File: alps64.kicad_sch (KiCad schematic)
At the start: 27 parts, among them J2 USB_C_Receptacle, K18 keyboard_parts:KEYSW, K19 keyboard_parts:KEYSW, K28 keyboard_parts:KEYSW, K29 keyboard_parts:KEYSW, K8 keyboard_parts:KEYSW, K9 keyboard_parts:KEYSW, SW100 SW_PUSH, U1 32U2, X1 16MHz

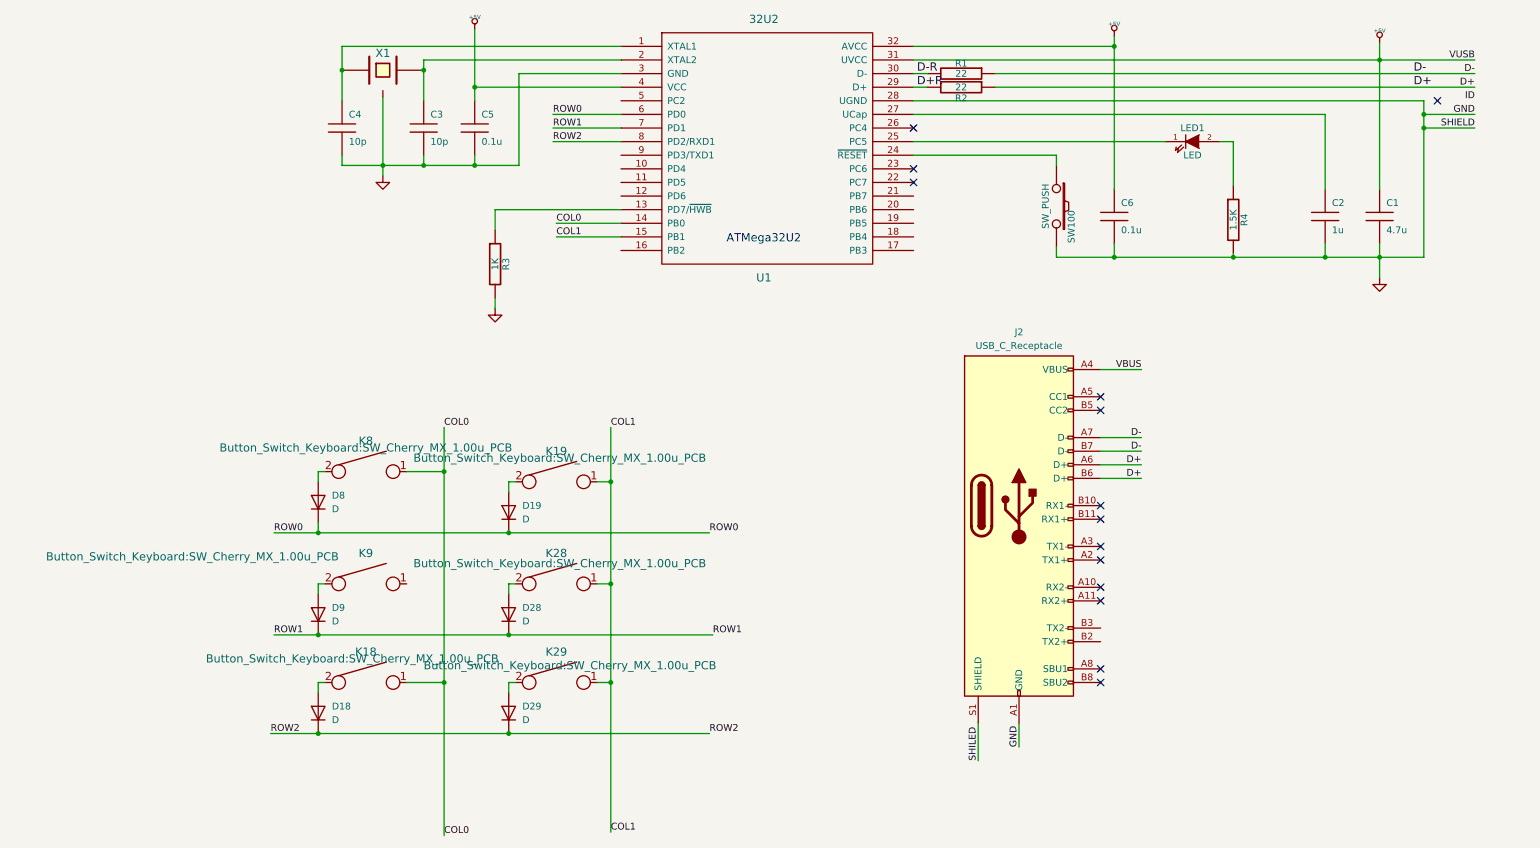
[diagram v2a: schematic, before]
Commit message: Update footprints
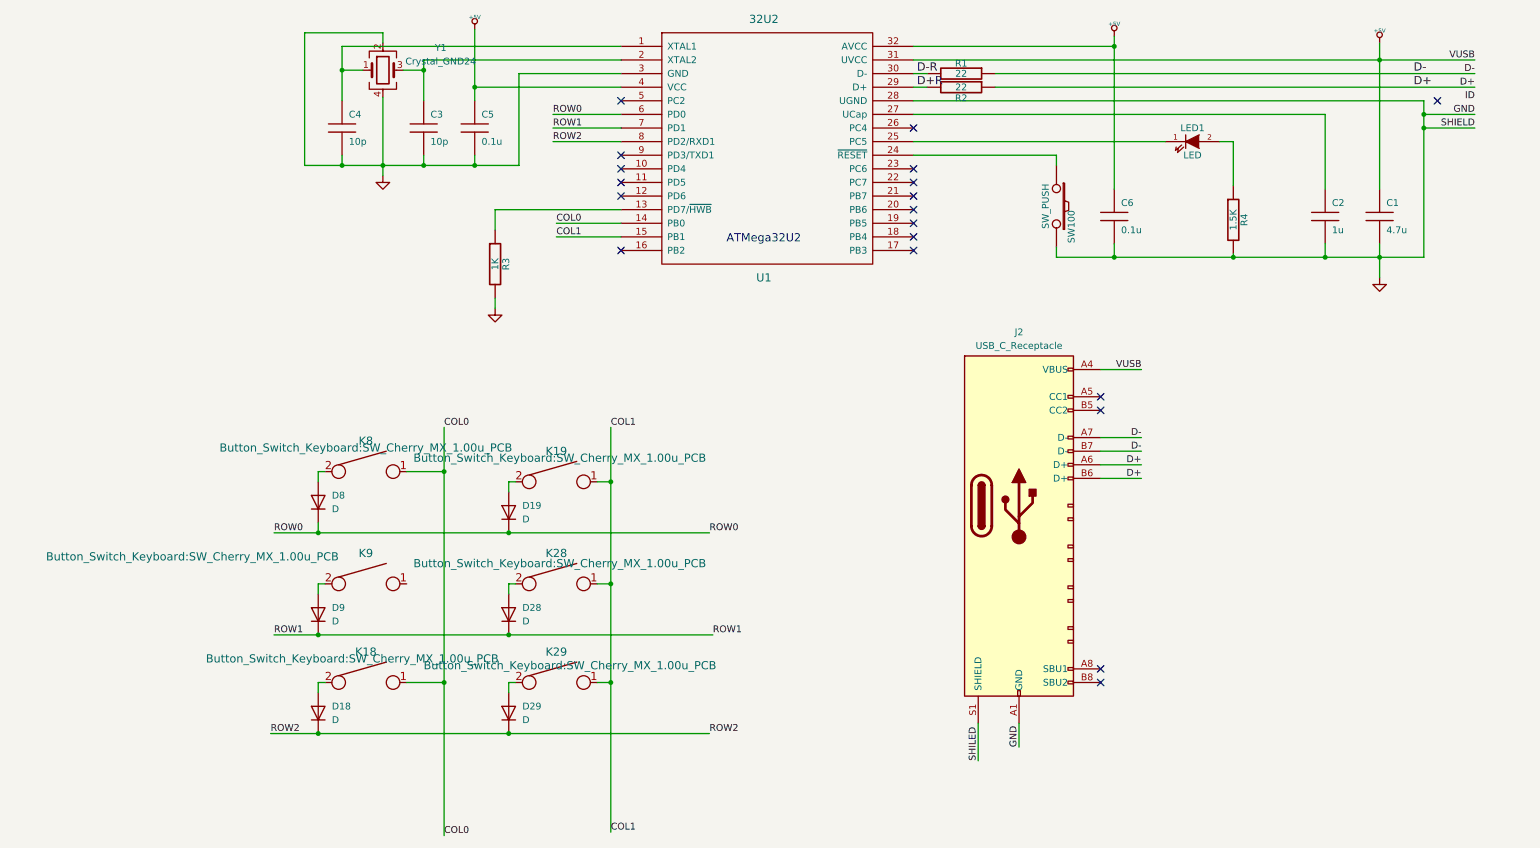
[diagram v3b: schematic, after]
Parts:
- removed X1: 16MHz, Crystal:Crystal_SMD_3225-4Pin_3.2x2.5mm, symbol alps64-rescue:XTAL_GND-keyboard_parts
- added Y1: Crystal_GND24, Crystal:Crystal_SMD_3225-4Pin_3.2x2.5mm, symbol Device:Crystal_GND24
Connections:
- net VBUS is gone; now on net +5V: J2.A4 (VBUS), J2.A9 (VBUS), J2.B4 (VBUS), J2.B9 (VBUS)
- net GND: now also Y1.2, Y1.4
- net at C4.1, U1.1 (XTAL1): now also Y1.1
- net at C3.1, U1.2 (XTAL2): now also Y1.3
- no-connect marks 14 -> 19
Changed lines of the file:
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@@
   (junction (at 73.025 151.765) (diameter 0) (color 0 0 0 0)
   )
+  (junction (at 53.975 37.465) (diameter 0) (color 0 0 0 0)
+  )
   (junction (at 198.12 72.39) (diameter 0) (color 0 0 0 0)
   )
-  (junction (at 53.975 37.465) (diameter 0) (color 0 0 0 0)
-  )
   (junction (at 78.74 55.245) (diameter 0) (color 0 0 0 0)
   )
+  (junction (at 53.975 55.245) (diameter 0) (color 0 0 0 0)
+  )
+  (junction (at 69.215 55.245) (diameter 0) (color 0 0 0 0)
+  )
+  (junction (at 78.74 40.64) (diameter 0) (color 0 0 0 0)
+  )
+  (junction (at 49.53 142.875) (diameter 0) (color 0 0 0 0)
+  )
+  (junction (at 104.14 114.3) (diameter 0) (color 0 0 0 0)
+  )
+  (junction (at 85.09 142.875) (diameter 0) (color 0 0 0 0)
+  )
   (junction (at 69.215 37.465) (diameter 0) (color 0 0 0 0)
   )
-  (junction (at 69.215 55.245) (diameter 0) (color 0 0 0 0)
-  )
-  (junction (at 78.74 40.64) (diameter 0) (color 0 0 0 0)
-  )
-  (junction (at 49.53 142.875) (diameter 0) (color 0 0 0 0)
-  )
-  (junction (at 104.14 114.3) (diameter 0) (color 0 0 0 0)
-  )
-  (junction (at 85.09 142.875) (diameter 0) (color 0 0 0 0)
-  )
-  (no_connect (at 195.58 121.285))
   (no_connect (at 160.655 48.26))
-  (no_connect (at 195.58 118.745))
-  (no_connect (at 195.58 133.985))
-  (no_connect (at 195.58 136.525))
-  (no_connect (at 195.58 128.905))
+  (no_connect (at 106.045 53.34))
   (no_connect (at 160.655 58.42))
   (no_connect (at 195.58 151.765))
+  (no_connect (at 106.045 43.18))
   (no_connect (at 195.58 100.965))
-  (no_connect (at 195.58 126.365))
+  (no_connect (at 160.655 71.12))
+  (no_connect (at 160.655 63.5))
+  (no_connect (at 106.045 60.96))
   (no_connect (at 160.655 55.88))
+  (no_connect (at 106.045 58.42))
   (no_connect (at 258.445 43.18))
+  (no_connect (at 160.655 60.96))
+  (no_connect (at 106.045 71.12))
   (no_connect (at 195.58 149.225))
+  (no_connect (at 160.655 68.58))
   (no_connect (at 195.58 98.425))
+  (no_connect (at 106.045 55.88))
+  (no_connect (at 160.655 66.04))
   (wire (pts (xy 85.09 133.35) (xy 85.09 135.255))
     (stroke (width 0) (type default))
   )
+  (wire (pts (xy 61.595 30.48) (xy 46.99 30.48))
+    (stroke (width 0) (type default))
+  )
   (wire (pts (xy 207.645 50.8) (xy 160.655 50.8))
     (stroke (width 0) (type default))
@@
     (stroke (width 0) (type default))
   )
+  (wire (pts (xy 53.975 37.465) (xy 53.975 43.18))
+    (stroke (width 0) (type default))
+  )
   (wire (pts (xy 49.53 123.825) (xy 85.09 123.825))
     (stroke (width 0) (type default))
@@
     (stroke (width 0) (type default))
   )
+  (wire (pts (xy 53.975 37.465) (xy 57.785 37.465))
+    (stroke (width 0) (type default))
+  )
   (wire (pts (xy 255.905 48.26) (xy 255.905 45.72))
     (stroke (width 0) (type default))
   )
+  (wire (pts (xy 46.99 55.245) (xy 53.975 55.245))
+    (stroke (width 0) (type default))
+  )
   (wire (pts (xy 82.55 80.01) (xy 82.55 81.915))
     (stroke (width 0) (type default))
   )
+  (wire (pts (xy 65.405 37.465) (xy 69.215 37.465))
+    (stroke (width 0) (type default))
+  )
   (wire (pts (xy 50.8 133.35) (xy 49.53 133.35))
     (stroke (width 0) (type default))
@@
     (stroke (width 0) (type default))
   )
+  (wire (pts (xy 46.99 30.48) (xy 46.99 55.245))
+    (stroke (width 0) (type default))
+  )
+  (wire (pts (xy 61.595 32.385) (xy 61.595 30.48))
+    (stroke (width 0) (type default))
+  )
   (wire (pts (xy 73.025 104.14) (xy 73.025 112.395))
     (stroke (width 0) (type default))
@@
     (stroke (width 0) (type default))
   )
+  (wire (pts (xy 69.215 37.465) (xy 69.215 43.18))
+    (stroke (width 0) (type default))
+  )
   (wire (pts (xy 255.905 72.39) (xy 255.905 48.26))
     (stroke (width 0) (type default))
@@
     (stroke (width 0) (type default))
   )
-  (wire (pts (xy 53.975 37.465) (xy 53.975 43.18))
-    (stroke (width 0) (type default))
-  )
   (wire (pts (xy 160.655 45.72) (xy 237.49 45.72))
     (stroke (width 0) (type default))
@@
   )
   (wire (pts (xy 198.12 31.115) (xy 198.12 33.02))
-    (stroke (width 0) (type default))
-  )
-  (wire (pts (xy 69.215 37.465) (xy 69.215 43.18))
     (stroke (width 0) (type default))
   )
@@
     (effects (font (size 1.27 1.27)) (justify right bottom))
   )
-  (label "VBUS" (at 203.2 93.345 180) (fields_autoplaced)
+  (label "VUSB" (at 203.2 93.345 180) (fields_autoplaced)
     (effects (font (size 1.27 1.27)) (justify right bottom))
   )
@@
     )
   )
-  (symbol (lib_id "alps64-rescue:XTAL_GND-keyboard_parts") (at 61.595 37.465 0) (unit 1)
-    (in_bom yes) (on_board yes) (dnp no)
-    (property "Reference" "X1" (at 61.595 34.29 0)
-      (effects (font (size 1.524 1.524)))
-    )
-    (property "Value" "16MHz" (at 61.595 32.7406 0)
-      (effects (font (size 1.524 1.524)) hide)
-    )
-    (property "Footprint" "Crystal:Crystal_SMD_3225-4Pin_3.2x2.5mm" (at 61.595 37.465 0)
-      (effects (font (size 1.524 1.524)) hide)
-    )
-    (property "Datasheet" "" (at 61.595 37.465 0)
-      (effects (font (size 1.524 1.524)))
-    )
-    (pin "1")
-    (pin "2")
-    (pin "3")
-    (instances
-      (project "alps64"
-        (path "/4b4949b7-9a63-426a-951a-a513f23d36ae"
-          (reference "X1") (unit 1)
-        )
-      )
-    )
-  )
   (symbol (lib_id "Device:D") (at 49.53 139.065 90) (unit 1)
     (in_bom yes) (on_board yes) (dnp no) (fields_autoplaced)
@@
     )
   )
+  (symbol (lib_id "Device:Crystal_GND24") (at 61.595 37.465 0) (unit 1)
+    (in_bom yes) (on_board yes) (dnp no) (fields_autoplaced)
+    (property "Reference" "Y1" (at 72.39 33.2741 0)
+      (effects (font (size 1.27 1.27)))
+    )
+    (property "Value" "Crystal_GND24" (at 72.39 35.8141 0)
+      (effects (font (size 1.27 1.27)))
+    )
+    (property "Footprint" "Crystal:Crystal_SMD_3225-4Pin_3.2x2.5mm" (at 61.595 37.465 0)
+      (effects (font (size 1.27 1.27)) hide)
+    )
+    (property "Datasheet" "~" (at 61.595 37.465 0)
+      (effects (font (size 1.27 1.27)) hide)
+    )
+    (pin "1")
+    (pin "2")
+    (pin "3")
+    (pin "4")
+    (instances
+      (project "alps64"
+        (path "/4b4949b7-9a63-426a-951a-a513f23d36ae"
+          (reference "Y1") (unit 1)
+        )
+      )
+    )
+  )
   (symbol (lib_id "Connector:USB_C_Receptacle") (at 180.34 118.745 0) (unit 1)
     (in_bom yes) (on_board yes) (dnp no) (fields_autoplaced)
@@
     )
     (pin "A1")
-    (pin "A10")
-    (pin "A11")
     (pin "A12")
-    (pin "A2")
-    (pin "A3")
     (pin "A4")
     (pin "A5")
@@
     (pin "A9")
     (pin "B1")
-    (pin "B10")
-    (pin "B11")
     (pin "B12")
-    (pin "B2")
-    (pin "B3")
     (pin "B4")
     (pin "B5")

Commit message: Update parts footprint
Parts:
- LED1: footprint LED_THT:LED_D1.8mm_W3.3mm_H2.4mm -> LED_SMD:LED_0805_2012Metric_Pad1.15x1.40mm_HandSolder
- R1, R2, R3, R4: footprint Resistor_THT:R_Axial_DIN0204_L3.6mm_D1.6mm_P7.62mm_Horizontal -> Resistor_SMD:R_0603_1608Metric
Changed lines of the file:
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@@
       (effects (font (size 1.27 1.27)))
     )
-    (property "Footprint" "Resistor_THT:R_Axial_DIN0204_L3.6mm_D1.6mm_P7.62mm_Horizontal" (at 169.545 40.64 0)
+    (property "Footprint" "Resistor_SMD:R_0603_1608Metric" (at 169.545 40.64 0)
       (effects (font (size 1.524 1.524)) hide)
     )
@@
       (effects (font (size 1.27 1.27)))
     )
-    (property "Footprint" "Resistor_THT:R_Axial_DIN0204_L3.6mm_D1.6mm_P7.62mm_Horizontal" (at 169.545 38.1 0)
+    (property "Footprint" "Resistor_SMD:R_0603_1608Metric" (at 169.545 38.1 0)
       (effects (font (size 1.524 1.524)) hide)
     )
@@
       (effects (font (size 1.27 1.27)))
     )
-    (property "Footprint" "Resistor_THT:R_Axial_DIN0204_L3.6mm_D1.6mm_P7.62mm_Horizontal" (at 82.55 73.66 0)
+    (property "Footprint" "Resistor_SMD:R_0603_1608Metric" (at 82.55 73.66 0)
       (effects (font (size 1.524 1.524)) hide)
     )
@@
       (effects (font (size 1.27 1.27)))
     )
-    (property "Footprint" "Resistor_THT:R_Axial_DIN0204_L3.6mm_D1.6mm_P7.62mm_Horizontal" (at 220.345 65.405 0)
+    (property "Footprint" "Resistor_SMD:R_0603_1608Metric" (at 220.345 65.405 0)
       (effects (font (size 1.524 1.524)) hide)
     )
@@
       (effects (font (size 1.27 1.27)))
     )
-    (property "Footprint" "LED_THT:LED_D1.8mm_W3.3mm_H2.4mm" (at 212.725 50.8 0)
-      (effects (font (size 1.524 1.524)) hide)
-    )
+    (property "Footprint" "LED_SMD:LED_0805_2012Metric_Pad1.15x1.40mm_HandSolder" (at 212.725 50.8 0)
+      (effects (font (size 1.524 1.524)) hide)
+    )

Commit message: Use through hall led footprint
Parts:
- LED1: footprint LED_SMD:LED_0805_2012Metric_Pad1.15x1.40mm_HandSolder -> LED_THT:LED_D3.0mm
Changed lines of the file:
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@@
       (effects (font (size 1.27 1.27)))
     )
-    (property "Footprint" "LED_SMD:LED_0805_2012Metric_Pad1.15x1.40mm_HandSolder" (at 212.725 50.8 0)
+    (property "Footprint" "LED_THT:LED_D3.0mm" (at 212.725 50.8 0)
       (effects (font (size 1.524 1.524)) hide)
     )
